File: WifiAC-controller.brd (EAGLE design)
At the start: 59.7 x 39.4 mm, 12 parts

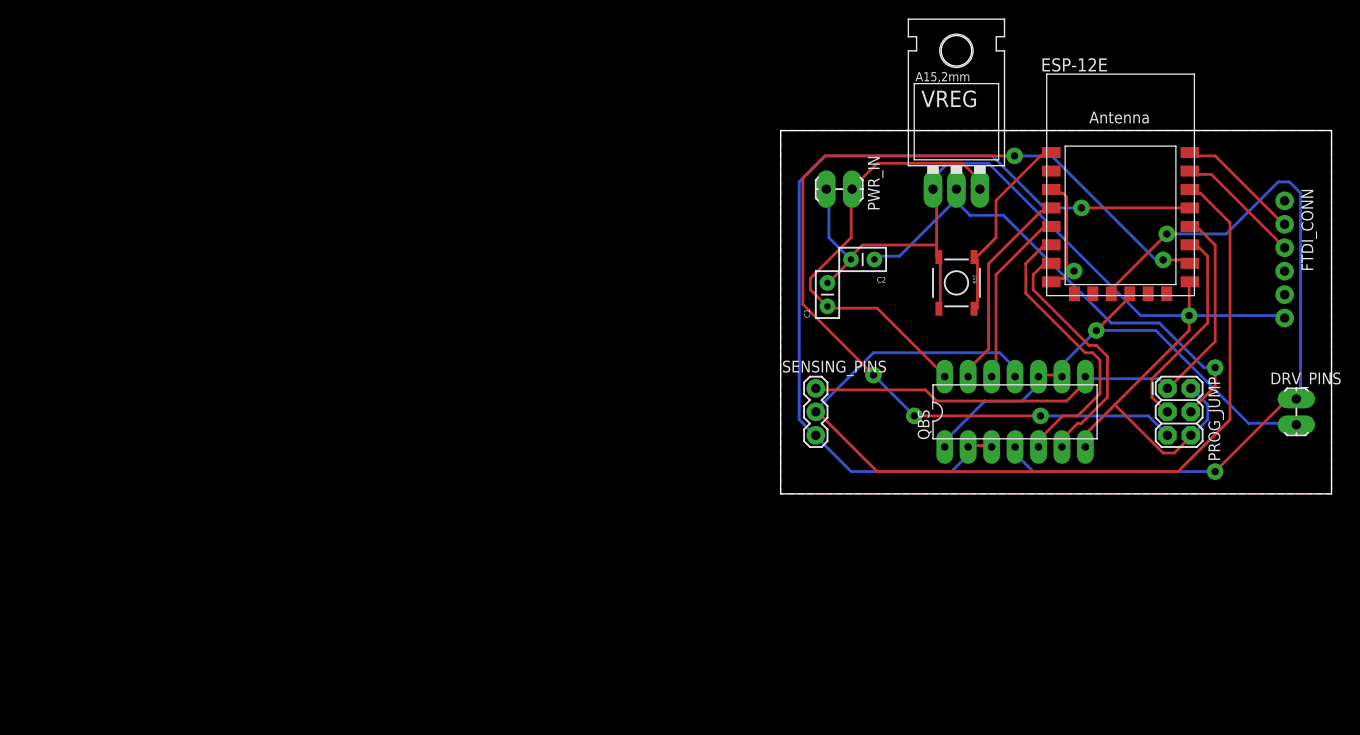
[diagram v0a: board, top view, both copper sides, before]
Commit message: changing to generic esp but the circuit is not done
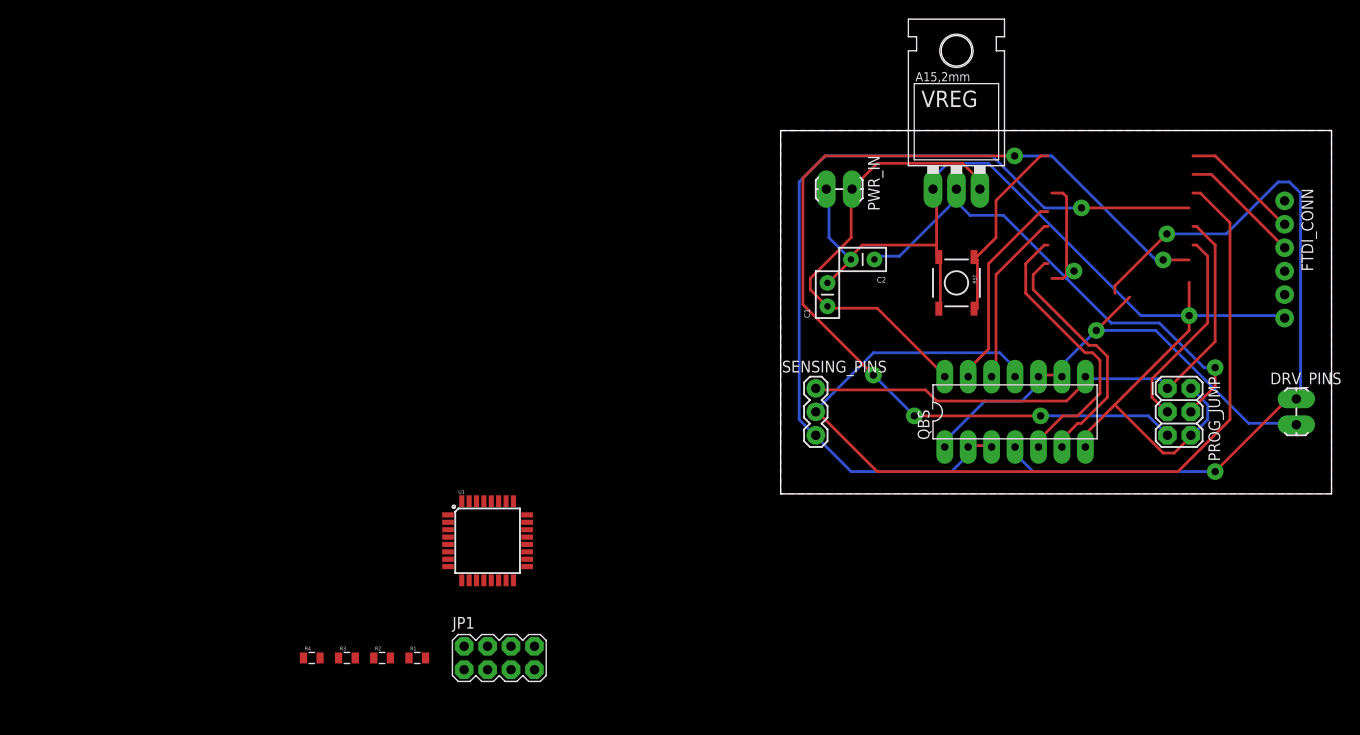
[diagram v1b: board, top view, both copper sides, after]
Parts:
- removed ESP-12E: ESP-07/12, ESP-12E:ESP-12E
- added JP1: (no value), SparkFun-Connectors:2X4
- added R1, R2, R3, R4: (no value), SparkFun-Passives:0805
- added U1: ATMEGA328P_TQFP, SparkFun-DigitalIC:TQFP32-08
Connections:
- net 3V3: no longer ESP-12E.3, ESP-12E.8
- net GND: no longer ESP-12E.9
- net GPIO12: no longer ESP-12E.6
- net GPIO13: no longer ESP-12E.7
- net GPIO14: no longer ESP-12E.5
- net GPIO15: no longer ESP-12E.10
- net GPIO16: no longer ESP-12E.4
- net GPIO2: no longer ESP-12E.11
- net N$1: no longer ESP-12E.1
- net P5: no longer ESP-12E.12
- net P58: no longer ESP-12E.19
- net P59: no longer ESP-12E.20
- net P6: no longer ESP-12E.14
- net P7: no longer ESP-12E.13
- net RX: no longer ESP-12E.16
- net TX: no longer ESP-12E.15
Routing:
- net 3V3: track 70.2 -> 69.5 mm
- net GPIO16: track 22.5 -> 21.9 mm
- net P6: track 103.0 -> 102.5 mm
- net N$1: track 21.5 -> 21.0 mm
- net TX: track 13.7 -> 13.2 mm

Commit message: updated the circuit and the output file. circuit update includes changing the esp package and adding an atmega328 as mcu
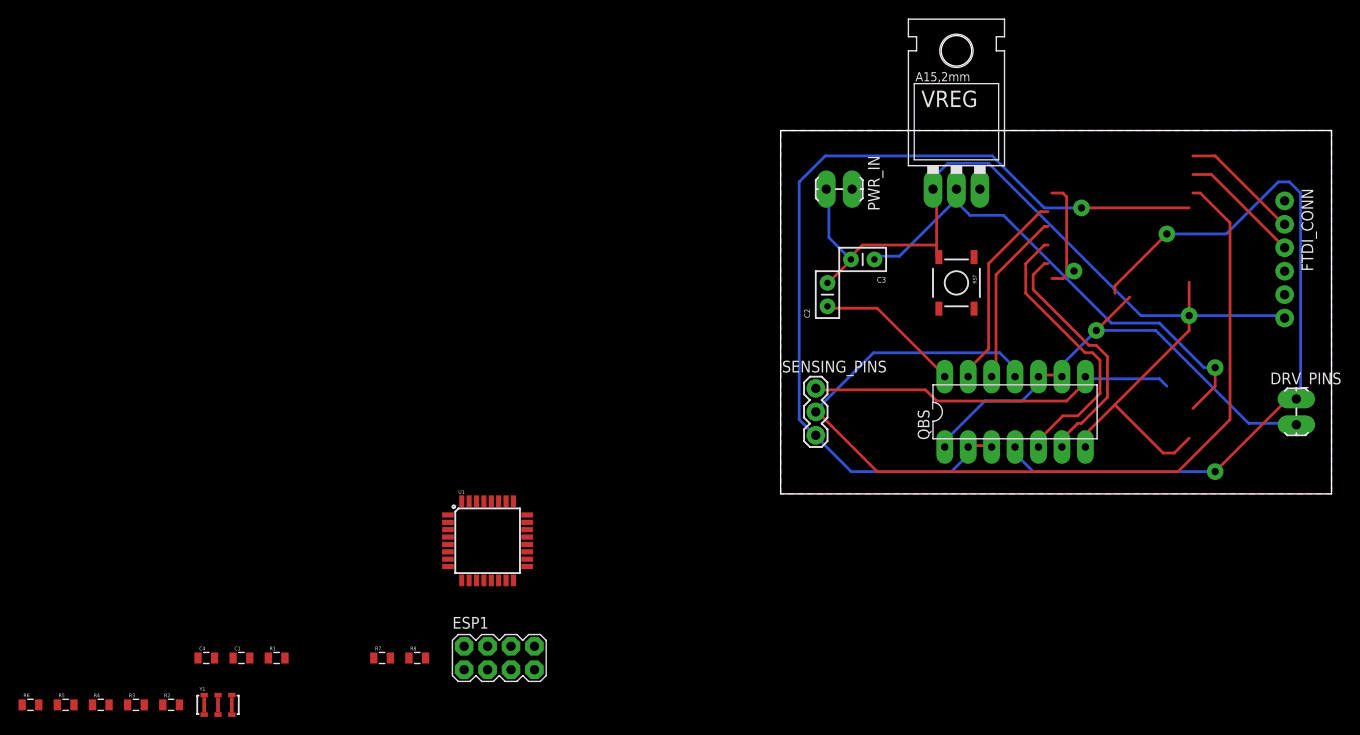
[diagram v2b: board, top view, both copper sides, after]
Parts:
- removed PROG_JUMP: FEMALE 2x3, SparkFun-Connectors:2X3
- added C3: 33u, SparkFun-Passives:CAP-PTH-SMALL2
- added C4: 0.1uF, SparkFun-Passives:0805
- added R5, R6: 510, SparkFun-Passives:0805
- added R7: 2K, SparkFun-Passives:0805
- added R8: 1K, SparkFun-Passives:0805
- added Y1: 4MHz, SparkFun-FreqCtrl:RESONATOR-SMD_MED
- C1: value 0.47u -> 0.1uF; device SparkFun-Passives:CAP-PTH-SMALLEZ -> SparkFun-Passives:0805
- C2: value 33u -> 0.47u; device SparkFun-Passives:CAP-PTH-SMALL2 -> SparkFun-Passives:CAP-PTH-SMALLEZ
- R1: value (none) -> 10K
- R2, R3, R4: value (none) -> 510
- RST: device SparkFun-Retired:TACTILE-SWITCH-SMD -> SparkFun-Electromechanical:TACTILE-SWITCH-SMD
- moved C1 74.1 mm to (-58.4, -17.8), turned to 0 degrees
- moved R2 23.4 mm to (-66.0, -22.9)
- moved R4 23.4 mm to (-73.7, -22.9)
- moved R3 23.4 mm to (-69.8, -22.9)
- moved R1 15.2 mm to (-54.6, -17.8)
- moved C2 7.18 mm to (5.08, 20.3), turned to 90 degrees
- renumbered JP1 to ESP1
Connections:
- removed net 5V: C1.1, PWR_IN.1, QBS_.14, VREG.OUT
- removed net GPIO12: QBS_.5
- removed net GPIO13: QBS_.6
- removed net GPIO14: QBS_.12
- removed net GPIO15: PROG_JUMP.5
- removed net GPIO16: QBS_.13
- removed net GPIO2: PROG_JUMP.3
- removed net RX: FTDI_CONN.2
- removed net TX: FTDI_CONN.3
- new net DTR: C1.1, FTDI_CONN.1
- new net DWN: QBS_.12, U1.17
- new net FAN: QBS_.5, U1.15
- new net N$10: R6.2, U1.11
- new net N$14: ESP1.8, R7.2, R8.1
- new net N$3: C4.1, U1.20
- new net N$4: U1.7, Y1.1
- new net N$5: U1.8, Y1.3
- new net N$6: R2.1, U1.32
- new net N$7: R3.1, U1.1
- new net N$8: R4.1, U1.9
- new net N$9: R5.1, U1.10
- new net PWR: QBS_.13, U1.14
- new net RXI: ESP1.1, FTDI_CONN.3, U1.30
- new net TXO: FTDI_CONN.2, R8.2, U1.31
- new net UP: QBS_.6, U1.16
- new net VCC: C2.1, FTDI_CONN.4, PWR_IN.1, QBS_.14, R1.2, U1.18, U1.4, U1.6, VREG.OUT
- net 3V3: now also C3.1, ESP1.3, ESP1.7; no longer C2.1, PROG_JUMP.4
- net GND: now also C3.2, C4.2, ESP1.2, FTDI_CONN.5, R7.1, U1.21, U1.3, U1.5, Y1.2; no longer C1.2, PROG_JUMP.2, PROG_JUMP.6
- net N$1: now also C1.2, R1.1, U1.29
- net P5: now also R4.2; no longer PROG_JUMP.1
- net P58: now also R2.2
- net P59: now also R3.2
- net P6: now also R5.2
- net P7: now also R6.1
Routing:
- net GPIO15: track 106.6 -> 0.00 mm, vias 5 -> 0
- net 5V: track 48.0 -> 0.00 mm
- net GPIO12: track 30.7 -> 0.00 mm
- net FAN: track 0.00 -> 30.7 mm
- net UP: track 0.00 -> 26.8 mm
- net GPIO13: track 26.8 -> 0.00 mm
- net GPIO2: track 22.2 -> 0.00 mm
- net PWR: track 0.00 -> 21.9 mm
- net GPIO16: track 21.9 -> 0.00 mm
- net P5: track 62.0 -> 40.8 mm
- net N$1: track 21.0 -> 0.00 mm
- net GPIO14: track 19.0 -> 0.00 mm
- net DWN: track 0.00 -> 19.0 mm
- net VCC: track 0.00 -> 15.7 mm
- net TX: track 13.2 -> 0.00 mm
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
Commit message: reouted the pcb
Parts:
- removed ESP1: (no value), SparkFun-Connectors:2X4
- removed _REFERENCE_HOLE_: (no value), WifiAC-controller~~~ref_tmp:_REFERENCE_HOLE_
- added ESP8266: (no value), SparkFun-Connectors:2X4
- C2: device SparkFun-Passives:CAP-PTH-SMALLEZ -> SparkFun-Passives:0805
- C3: device SparkFun-Passives:CAP-PTH-SMALL2 -> SparkFun-Passives:0805
- DRV_PINS, PWR_IN: device SparkFun-Connectors:1X02_LOCK_LONGPADS -> SparkFun-Connectors:MOLEX-1X2
- SENSING_PINS: device SparkFun-Connectors:1X03 -> SparkFun-Connectors:MOLEX-1X3
- moved R4 122.1 mm to (34.3, 34.3)
- moved R5 121.0 mm to (29.2, 34.3), turned to 180 degrees
- moved Y1 108.1 mm to (38.1, 20.3)
- moved R6 107.7 mm to (21.6, 8.89), turned to 90 degrees
- moved R3 103.8 mm to (26.7, 15.2), turned to 270 degrees
- moved R2 97.1 mm to (21.6, 19.1), turned to 270 degrees
- moved C4 93.3 mm to (19.1, 27.9), turned to 180 degrees
- moved R7 92.5 mm to (45.7, 7.62), turned to 90 degrees
- moved C1 91.2 mm to (29.2, 7.62), turned to 90 degrees
- moved R1 90.0 mm to (30.5, 11.4)
- moved R8 87.8 mm to (45.7, 3.81), turned to 90 degrees
- moved U1 67.6 mm to (27.9, 26.7), turned to 180 degrees
- moved FTDI_CONN 31.9 mm to (41.9, 2.54), turned to 180 degrees
- moved C2 16.6 mm to (14.0, 34.3), turned to 180 degrees
- moved RST 15.7 mm to (3.81, 19.1)
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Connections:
- net 3V3: now also ESP8266.3, ESP8266.7; no longer ESP1.3, ESP1.7
- net GND: now also ESP8266.2; no longer ESP1.2
- net N$14: now also ESP8266.8; no longer ESP1.8
- net P58: now also DRV_PINS.2; no longer DRV_PINS.1
- net P59: now also DRV_PINS.1; no longer DRV_PINS.2
- net RXI: now also ESP8266.1; no longer ESP1.1
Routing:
- net VCC: track 15.7 -> 148.4 mm, vias 0 -> 2
- net P7: track 96.4 -> 25.1 mm, vias 1 -> 0
- net N$1: track 0.00 -> 67.3 mm, vias 0 -> 4
- net P6: track 102.5 -> 54.1 mm, vias 0 -> 3
- net PWR: track 21.9 -> 68.5 mm, vias 0 -> 1
- net N$14: track 0.00 -> 33.5 mm
- net RXI: track 13.2 -> 44.8 mm, vias 0 -> 2
- net P58: track 83.8 -> 52.9 mm, vias 2 -> 0
- net N$10: track 0.00 -> 29.6 mm, vias 0 -> 2
- net GND: track 110.7 -> 139.8 mm, vias 1 -> 3
- net TXO: track 13.0 -> 41.5 mm, vias 0 -> 1
- net DWN: track 19.0 -> 41.1 mm, vias 0 -> 2
- net P5: track 40.8 -> 62.4 mm, vias 0 -> 1
- net N$5: track 0.00 -> 19.0 mm, vias 0 -> 2
- net DTR: track 0.00 -> 14.6 mm
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- added copper zone on layer 1, net GND
- removed copper zone on layer 1, net N$2
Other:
- board size 59.7 x 39.4 mm -> 50.8 x 36.8 mm

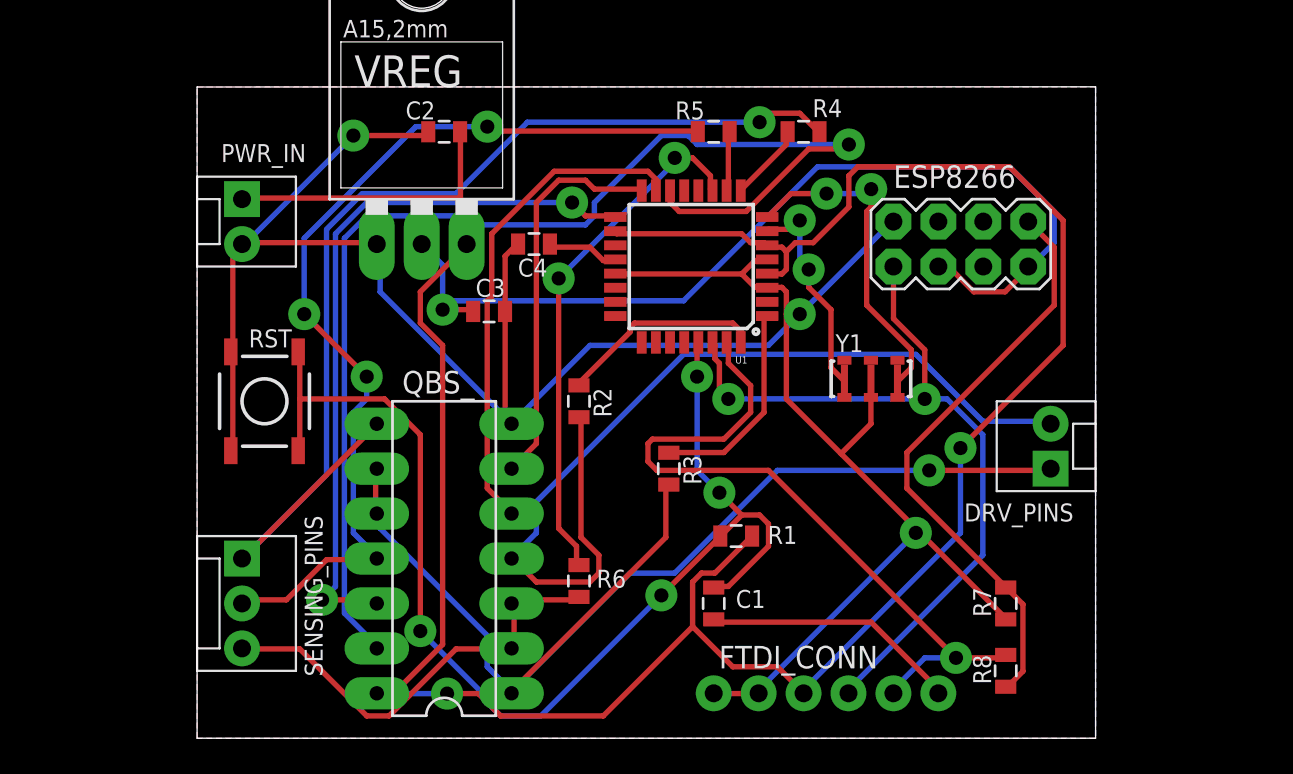
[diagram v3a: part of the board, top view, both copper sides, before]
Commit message: changed the wrong 0.2 clearance and rerouted the circuit
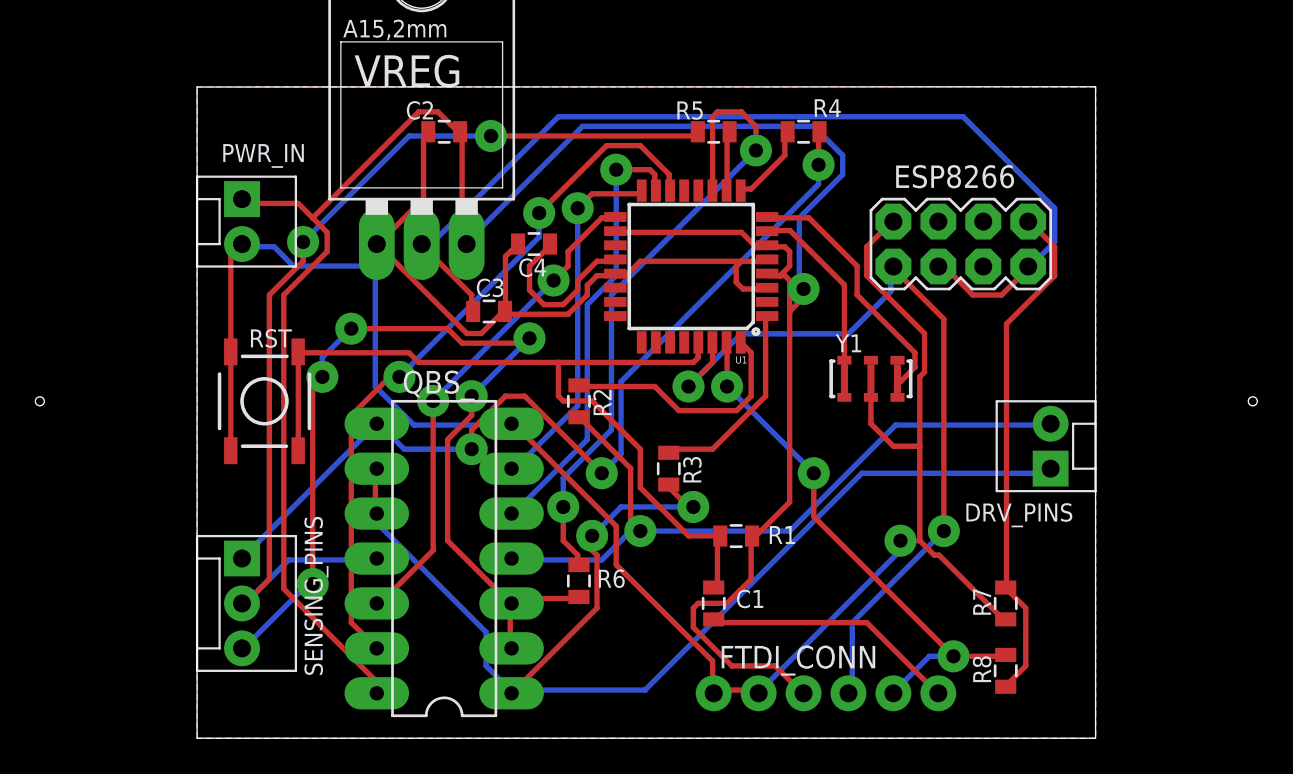
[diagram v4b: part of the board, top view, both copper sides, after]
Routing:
- net P7: track 25.1 -> 56.3 mm, vias 0 -> 5
- net PWR: track 68.5 -> 40.5 mm, vias 1 -> 2
- net N$1: track 67.3 -> 48.0 mm, vias 4 -> 0
- net VCC: track 148.4 -> 131.8 mm, vias 2 -> 1
- net DWN: track 41.1 -> 27.9 mm
- net P58: track 52.9 -> 41.6 mm, vias 0 -> 1
- net TXO: track 41.5 -> 30.3 mm, vias 1 -> 3
- net P5: track 62.4 -> 52.2 mm, vias 1 -> 3
- net N$10: track 29.6 -> 36.8 mm
- net GND: track 139.8 -> 146.6 mm, vias 3 -> 1
- net N$3: track 4.08 -> 9.62 mm
- net N$14: track 33.5 -> 29.0 mm
- net N$5: track 19.0 -> 14.7 mm, vias 2 -> 0
- net P59: track 67.2 -> 71.1 mm, vias 1 -> 2
- net FAN: track 28.1 -> 25.2 mm, vias 0 -> 1
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
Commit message: generated and optimized mill path
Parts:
- added _REFERENCE_HOLE_: (no value), WifiAC-controller~~~ref_tmp:_REFERENCE_HOLE_
